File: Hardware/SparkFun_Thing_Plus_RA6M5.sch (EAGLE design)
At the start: 109 parts, among them J1 USB Female Type C Connector, J2 THING_PLUS_LOGICAL, J3 QWIIC_RA, J4 CONN_03X2, J7 MICRO-SDFRICTION, Q1 20V/4.2A/52mΩ/1.4W, Q2 20V/4.2A/52mΩ/1.4W, U1 R7FA6M5, U2 DA14531MOD, U3 MCP73831, U4 RT9080-33GJ5, U5 W25QXX128MBIT-6X5, U6 RT9080-33GJ5, U7 MAX17048, U8 LM66200, Y1 24.000MHz, Y2 32.768kHz

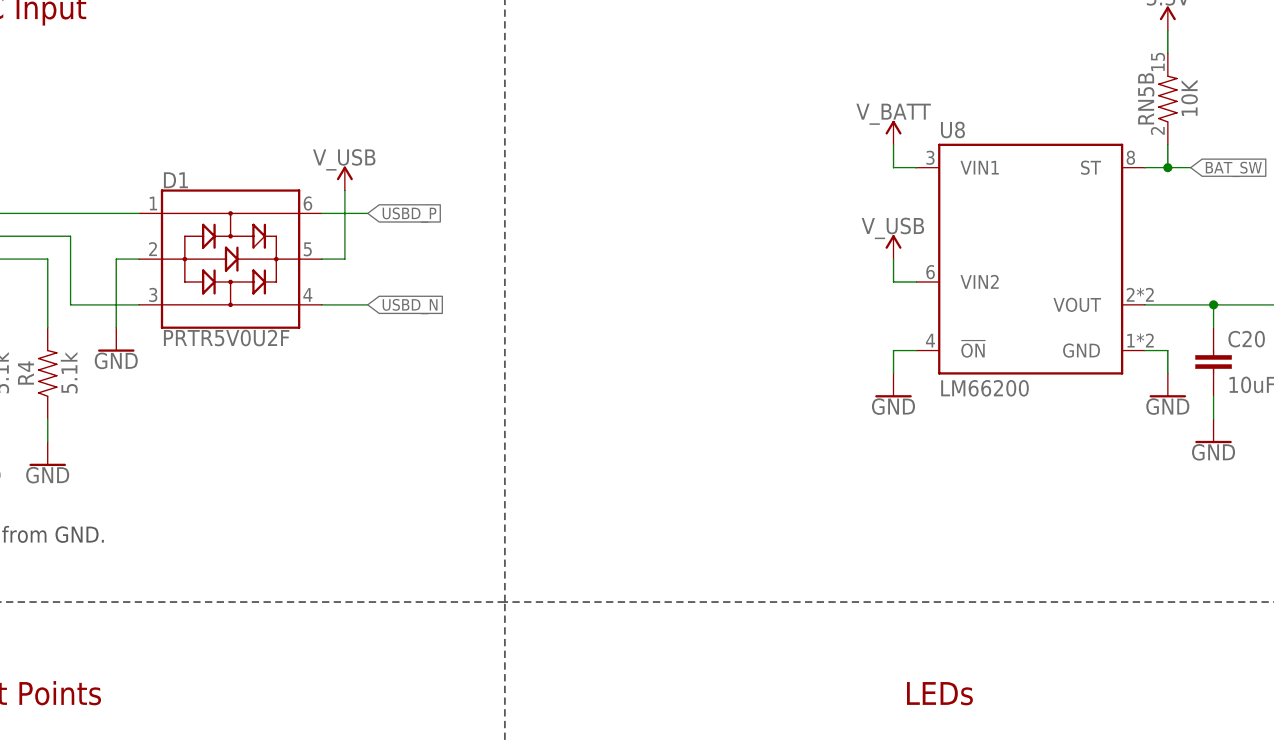
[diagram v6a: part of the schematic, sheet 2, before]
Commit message: Update post-design review.
Add USB diff calcs to schematic.
Add product name silk to bottom of board.
Consolidate 0.1u caps.
Stitch power and ground planes better.
Analyze PDN to chip and improve.
Pour 3V3 under USB on top and bot.
Space parts away to reduce crowding.
Increase TP sizes where possible.
Space out TPs where possible.
Space out pin silk.
Add a poly on L4 for 3V3.
Mod LM66200 sch symbol for clarity.
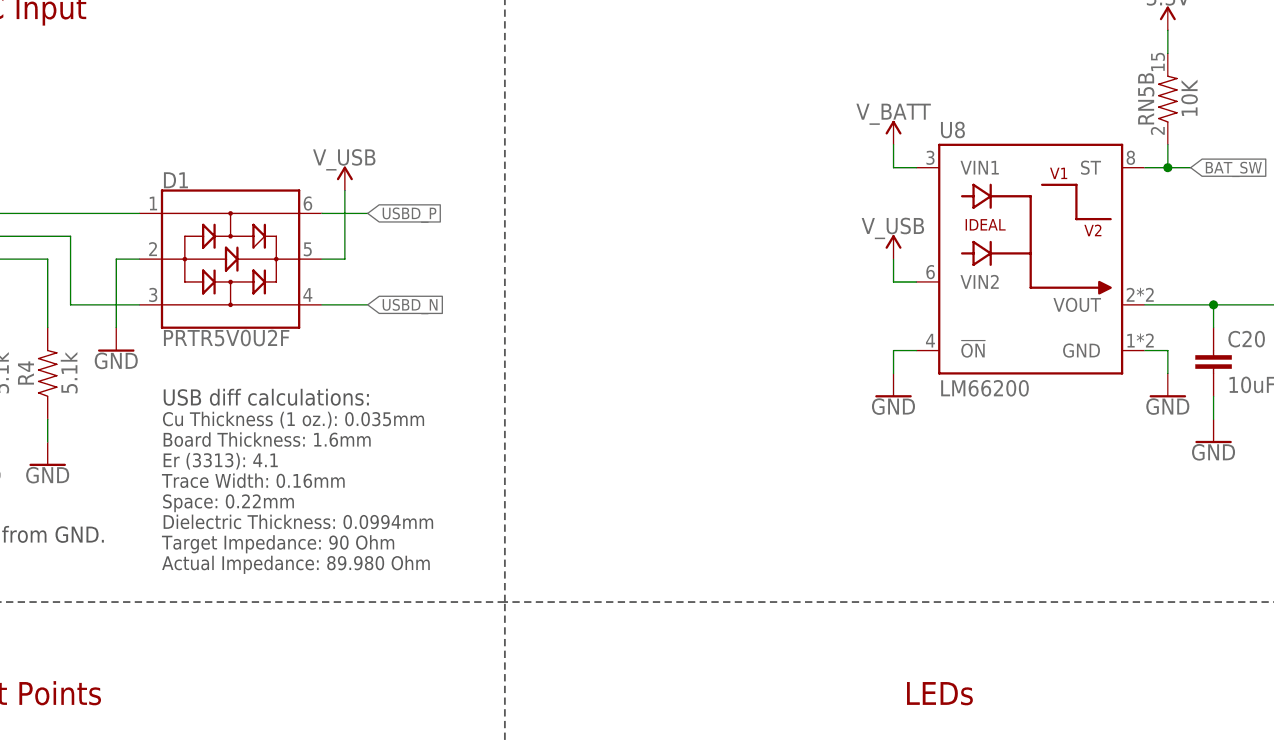
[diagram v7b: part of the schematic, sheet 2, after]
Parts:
- C11, C12, C2, C25, C26, C3, C4, C5, C6: device SparkFun-Capacitors:0.1UF-0402T-6.3V-10%-X7R -> SparkFun-Capacitors:0.1UF-0402T-16V-10%
- TP1, TP3, TP5, TP6, TP7, TP8: value TEST-POINT3X4 -> TEST-POINT3X5; device SparkFun-Connectors:TEST-POINT3X4 -> SparkFun-Connectors:TEST-POINT3X5
- TP9: value TEST-POINT3X4 -> TEST-POINT3; device SparkFun-Connectors:TEST-POINT3X4 -> SparkFun-Connectors:TEST-POINT3
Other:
- note added: "Cu Thickness (1 oz.): 0.035mm Board Thickness: 1.6mm Er (3313): 4.1 Trace Width: 0.16mm Space: 0.22mm Dielectric Thickness: 0.0994mm Target Impedance: 90 Ohm Actual Impedance: 89.980 Ohm"
- note added: "USB diff calculations:"
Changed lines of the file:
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@@
 <part name="C8" library="SparkFun-Capacitors" deviceset="DNP" device="-0402-TIGHT_NO_CREAM" value="DNP"/>
 <part name="SUPPLY4" library="SparkFun-PowerSymbols" deviceset="3.3V" device=""/>
-<part name="C5" library="SparkFun-Capacitors" deviceset="0.1UF" device="-0402T-6.3V-10%-X7R" value="0.1uF"/>
-<part name="C4" library="SparkFun-Capacitors" deviceset="0.1UF" device="-0402T-6.3V-10%-X7R" value="0.1uF"/>
-<part name="C3" library="SparkFun-Capacitors" deviceset="0.1UF" device="-0402T-6.3V-10%-X7R" value="0.1uF"/>
-<part name="C2" library="SparkFun-Capacitors" deviceset="0.1UF" device="-0402T-6.3V-10%-X7R" value="0.1uF"/>
-<part name="C6" library="SparkFun-Capacitors" deviceset="0.1UF" device="-0402T-6.3V-10%-X7R" value="0.1uF"/>
-<part name="C11" library="SparkFun-Capacitors" deviceset="0.1UF" device="-0402T-6.3V-10%-X7R" value="0.1uF"/>
+<part name="C5" library="SparkFun-Capacitors" deviceset="0.1UF" device="-0402T-16V-10%" value="0.1uF"/>
+<part name="C4" library="SparkFun-Capacitors" deviceset="0.1UF" device="-0402T-16V-10%" value="0.1uF"/>
+<part name="C3" library="SparkFun-Capacitors" deviceset="0.1UF" device="-0402T-16V-10%" value="0.1uF"/>
+<part name="C2" library="SparkFun-Capacitors" deviceset="0.1UF" device="-0402T-16V-10%" value="0.1uF"/>
+<part name="C6" library="SparkFun-Capacitors" deviceset="0.1UF" device="-0402T-16V-10%" value="0.1uF"/>
+<part name="C11" library="SparkFun-Capacitors" deviceset="0.1UF" device="-0402T-16V-10%" value="0.1uF"/>
 <part name="GND28" library="SparkFun-PowerSymbols" deviceset="GND" device=""/>
-<part name="C12" library="SparkFun-Capacitors" deviceset="0.1UF" device="-0402T-6.3V-10%-X7R" value="0.1uF"/>
+<part name="C12" library="SparkFun-Capacitors" deviceset="0.1UF" device="-0402T-16V-10%" value="0.1uF"/>
 <part name="GND29" library="SparkFun-PowerSymbols" deviceset="GND" device=""/>
 <part name="GND23" library="SparkFun-PowerSymbols" deviceset="GND" device=""/>
@@
 <part name="GND44" library="SparkFun-PowerSymbols" deviceset="GND" device=""/>
 <part name="SUPPLY40" library="SparkFun-PowerSymbols" deviceset="3.3V" device=""/>
-<part name="TP1" library="SparkFun-Connectors" deviceset="TEST-POINT" device="3X4" value="TEST-POINT3X4"/>
+<part name="TP1" library="SparkFun-Connectors" deviceset="TEST-POINT" device="3X5" value="TEST-POINT3X5"/>
 <part name="TP2" library="SparkFun-Connectors" deviceset="TEST-POINT" device="3X4" value="TEST-POINT3X4"/>
-<part name="TP3" library="SparkFun-Connectors" deviceset="TEST-POINT" device="3X4" value="TEST-POINT3X4"/>
+<part name="TP3" library="SparkFun-Connectors" deviceset="TEST-POINT" device="3X5" value="TEST-POINT3X5"/>
 <part name="TP4" library="SparkFun-Connectors" deviceset="TEST-POINT" device="3" value="TEST-POINT3"/>
-<part name="TP5" library="SparkFun-Connectors" deviceset="TEST-POINT" device="3X4" value="TEST-POINT3X4"/>
-<part name="TP6" library="SparkFun-Connectors" deviceset="TEST-POINT" device="3X4" value="TEST-POINT3X4"/>
-<part name="TP7" library="SparkFun-Connectors" deviceset="TEST-POINT" device="3X4" value="TEST-POINT3X4"/>
-<part name="TP8" library="SparkFun-Connectors" deviceset="TEST-POINT" device="3X4" value="TEST-POINT3X4"/>
+<part name="TP5" library="SparkFun-Connectors" deviceset="TEST-POINT" device="3X5" value="TEST-POINT3X5"/>
+<part name="TP6" library="SparkFun-Connectors" deviceset="TEST-POINT" device="3X5" value="TEST-POINT3X5"/>
+<part name="TP7" library="SparkFun-Connectors" deviceset="TEST-POINT" device="3X5" value="TEST-POINT3X5"/>
+<part name="TP8" library="SparkFun-Connectors" deviceset="TEST-POINT" device="3X5" value="TEST-POINT3X5"/>
 <part name="H3" library="SparkFun-Hardware" deviceset="STAND-OFF" device="TIGHT"/>
 <part name="H4" library="SparkFun-Hardware" deviceset="STAND-OFF" device="TIGHT"/>
@@
 <part name="C24" library="SparkFun-Capacitors" deviceset="47UF" device="" value="47uF/6.3V"/>
 <part name="GND50" library="SparkFun-PowerSymbols" deviceset="GND" device=""/>
-<part name="C25" library="SparkFun-Capacitors" deviceset="0.1UF" device="-0402T-6.3V-10%-X7R" value="0.1uF"/>
-<part name="C26" library="SparkFun-Capacitors" deviceset="0.1UF" device="-0402T-6.3V-10%-X7R" value="0.1uF"/>
+<part name="C25" library="SparkFun-Capacitors" deviceset="0.1UF" device="-0402T-16V-10%" value="0.1uF"/>
+<part name="C26" library="SparkFun-Capacitors" deviceset="0.1UF" device="-0402T-16V-10%" value="0.1uF"/>
 <part name="C27" library="SparkFun-Capacitors" deviceset="1.0UF" device="-0402T-16V-10%" value="1.0uF"/>
 <part name="U$5" library="SparkFun-PowerSymbols" deviceset="AGND" device=""/>
@@
 <part name="GND51" library="SparkFun-PowerSymbols" deviceset="GND" device=""/>
 <part name="SUPPLY45" library="SparkFun-PowerSymbols" deviceset="V_USB" device=""/>
-<part name="TP9" library="SparkFun-Connectors" deviceset="TEST-POINT" device="3X4" value="TEST-POINT3X4"/>
+<part name="TP9" library="SparkFun-Connectors" deviceset="TEST-POINT" device="3" value="TEST-POINT3"/>
 <part name="SUPPLY46" library="SparkFun-PowerSymbols" deviceset="3.3V" device=""/>
 <part name="RST" library="SparkFun-Jumpers" deviceset="JUMPER-SMT_2_NC_TRACE" device="_SILK" package3d_urn="urn:adsk.eagle:package:39281/1"/>
@@
 <wire x1="195.58" y1="134.62" x2="195.58" y2="200.66" width="0.1524" layer="97" style="longdash"/>
 <text x="149.86" y="53.34" size="2.54" layer="94" font="vector" align="center">SD Card Power Switch</text>
+<text x="63.5" y="222.504" size="1.778" layer="97" font="vector" ratio="15">USB diff calculations:</text>
+<text x="63.5" y="221.742" size="1.524" layer="97" font="vector" align="top-left">Cu Thickness (1 oz.): 0.035mm
+Board Thickness: 1.6mm
+Er (3313): 4.1
+Trace Width: 0.16mm
+Space: 0.22mm
+Dielectric Thickness: 0.0994mm
+Target Impedance: 90 Ohm
+Actual Impedance: 89.980 Ohm</text>
 </plain>
 <instances>

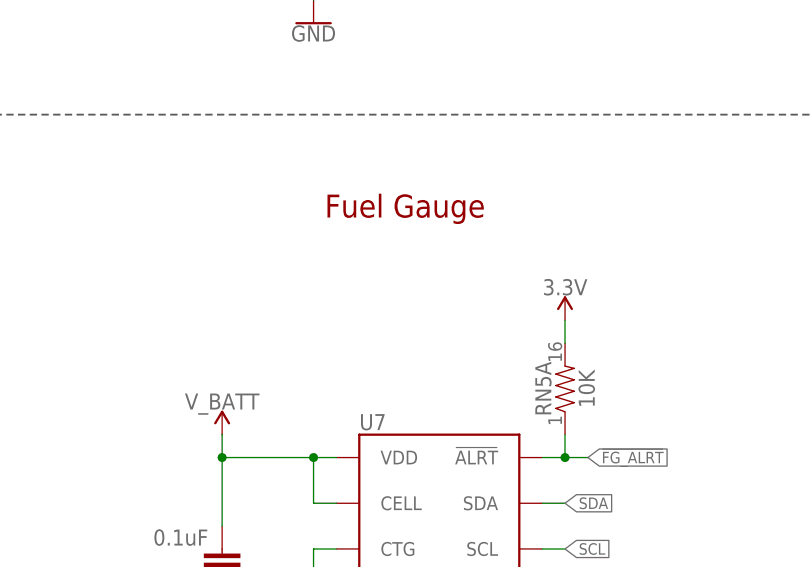
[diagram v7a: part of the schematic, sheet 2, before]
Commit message: Minor update to v01.
Add Fuel Gauge address text to schematic.
Add +/- silk for battery connector.
Re-export PDF.
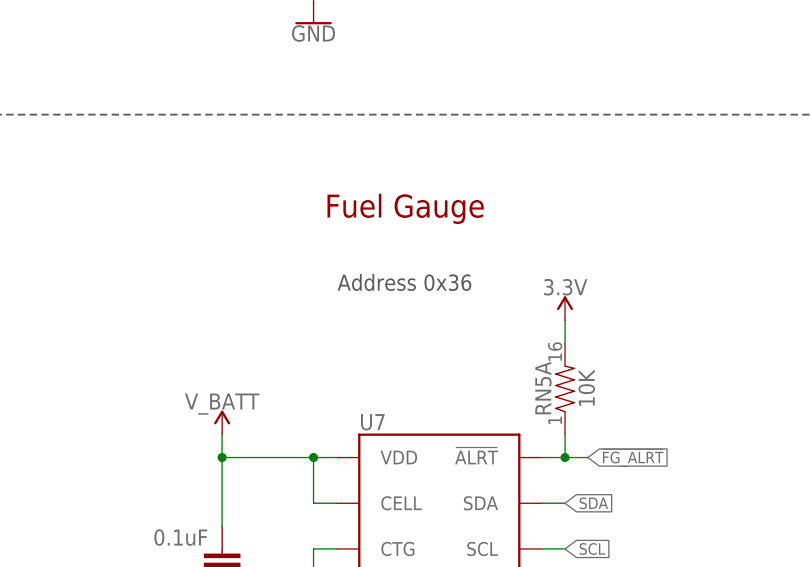
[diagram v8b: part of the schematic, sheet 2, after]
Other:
- note added: "Address 0x36"
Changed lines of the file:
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@@
 Target Impedance: 90 Ohm
 Actual Impedance: 89.980 Ohm</text>
+<text x="381" y="182.88" size="1.778" layer="97" font="vector" align="top-center">Address 0x36</text>
 </plain>
 <instances>
